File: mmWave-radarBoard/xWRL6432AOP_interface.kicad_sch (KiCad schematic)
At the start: 27 parts, among them U101 MX25R3235FZNxx0, U206 XI6432BRQAAMY, Y101 40MHz

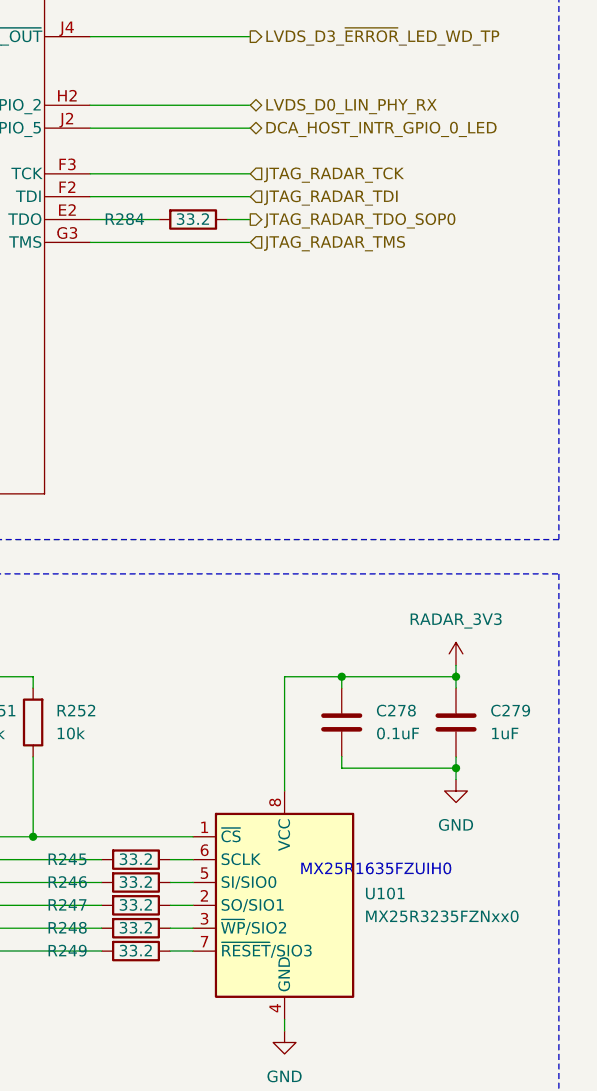
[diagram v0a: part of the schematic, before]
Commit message: Updated schematic of the radar module
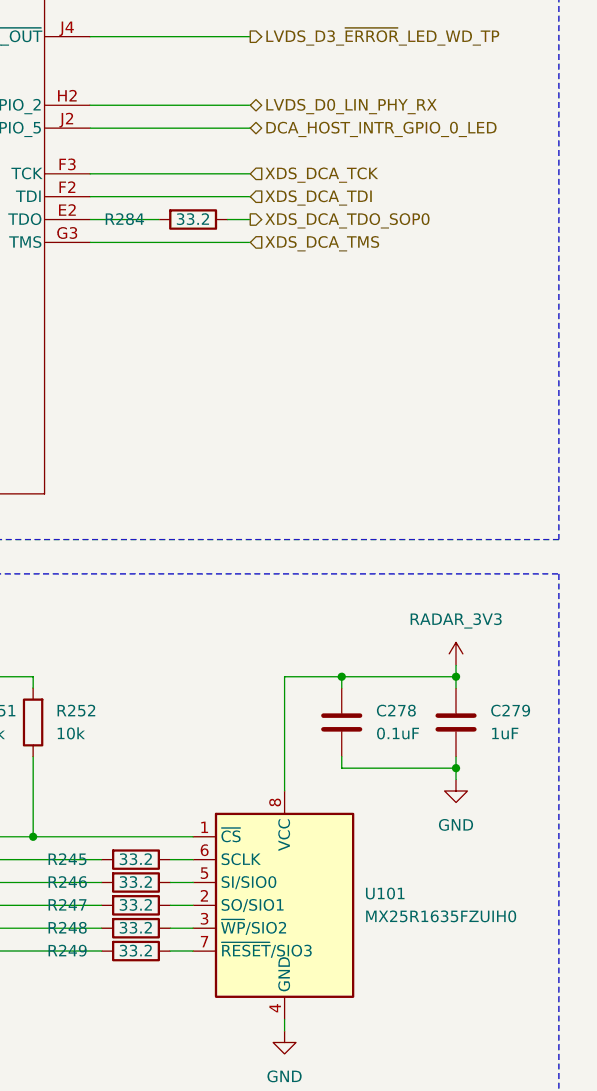
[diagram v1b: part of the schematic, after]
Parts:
- U101: value MX25R3235FZNxx0 -> MX25R1635FZUIH0
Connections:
- net JTAG_RADAR_TCK renamed XDS_DCA_TCK
- net JTAG_RADAR_TDI renamed XDS_DCA_TDI
- net JTAG_RADAR_TDO_SOP0 renamed XDS_DCA_TDO_SOP0
- net JTAG_RADAR_TMS renamed XDS_DCA_TMS
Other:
- note removed: "MX25R1635FZUIH0"
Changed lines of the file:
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@@
 		(company "Designer: EV")
 	)
-	(text "MX25R1635FZUIH0"
-		(exclude_from_sim no)
-		(at 218.44 138.43 0)
-		(effects
-			(font
-				(size 1.27 1.27)
-			)
-		)
-	)
 	(text_box "xWRL6432AOP QSPI flash"
 		(exclude_from_sim no)
@@
 		)
 	)
-	(hierarchical_label "JTAG_RADAR_TDO_SOP0"
+	(hierarchical_label "XDS_DCA_TDO_SOP0"
 		(shape output)
 		(at 204.47 66.04 0)
@@
 		)
 	)
-	(hierarchical_label "JTAG_RADAR_TDI"
+	(hierarchical_label "XDS_DCA_TDI"
 		(shape input)
 		(at 204.47 63.5 0)
@@
 		)
 	)
-	(hierarchical_label "JTAG_RADAR_TMS"
+	(hierarchical_label "XDS_DCA_TMS"
 		(shape input)
 		(at 204.47 68.58 0)
@@
 		)
 	)
-	(hierarchical_label "JTAG_RADAR_TCK"
+	(hierarchical_label "XDS_DCA_TCK"
 		(shape input)
 		(at 204.47 60.96 0)
@@
 			)
 		)
-		(property "Value" "MX25R3235FZNxx0"
+		(property "Value" "MX25R1635FZUIH0"
 			(at 217.17 143.5099 0)
 			(effects

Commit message: Removed unnecessary bits
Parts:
- added D501: LED RED, symbol Device:LED
- added R278: 2.2k, symbol Device:R
- added R279: 0, symbol Device:R
- added TP213, TP214, TP216: TestPoint, symbol Connector:TestPoint
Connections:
- net DCA_FTDI_MOSI renamed FTDI_MOSI
- net DCA_HOST_INTR_GPIO_0_LED renamed HOST_INTR_GPIO_0_LED
- net DCA_SPI_CLK_I2C_SCL renamed SPI_CLK_I2C_SCL
- net DCA_SPI_CLK_I2C_SDA renamed SPI_CLK_I2C_SDA
- net DCA_SPI_MISO_REG_MODE renamed SPI_MISO_REG_MODE
- net LVDS_CLK_RTC_CLKIN_TP renamed RTC_CLK
- net RTC_CLK: now also TP214.1
- net LVDS_D0_LIN_PHY_RX renamed LIN_PHY_RX
- net LVDS_D1_XDS_UARTA_RX_CAN_RX renamed CAN_RX
- net LVDS_D2_XDS_UARTA_TX_CAN_TX renamed CAN_TX
- net LVDS_D3_~{ERROR}_LED_WD_TP renamed ~{ERROR}_LED_WD_TP
- net ~{ERROR}_LED_WD_TP: now also D501.1 (K), R279.1, TP216.1
- net LVDS_FRCLK_HOST_CLK_TP renamed HOST_CLK
- net HOST_CLK: now also TP213.1
- net XDS_DCA_RS232_RX renamed RS232_RX
- net XDS_DCA_RS232_TX renamed RS232_TX
- net XDS_DCA_TCK renamed TCK
- net XDS_DCA_TDI renamed TDI
- net XDS_DCA_TDO_SOP0 renamed TDO_SOP0
- net XDS_DCA_TMS renamed TMS
- new net: D501.2 (A), R278.1
- new net VCC_3V3: R278.2, R279.2

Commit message: Finished schematic
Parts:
- added C502: 10uF, Capacitor_SMD:C_0603_1608Metric, symbol Device:C
- added J501: Conn_02x06_Odd_Even, Connector_JST:JST_PUD_B12B-PUDSS_2x06_P2.00mm_Vertical, symbol Connector_Generic:Conn_02x06_Odd_Even
- C501: renamed from C280; footprint (none) -> Capacitor_SMD:C_0603_1608Metric
- C503: renamed from C278; footprint (none) -> Capacitor_SMD:C_0603_1608Metric
- C504: renamed from C279; footprint (none) -> Capacitor_SMD:C_0603_1608Metric
- C505: renamed from C283; footprint (none) -> Capacitor_SMD:C_0402_1005Metric
- C506: renamed from C281; footprint (none) -> Capacitor_SMD:C_0402_1005Metric
- C507: renamed from C282; footprint (none) -> Capacitor_SMD:C_0402_1005Metric
- D501: footprint (none) -> LED_SMD:LED_0603_1608Metric
- R501: renamed from R253; footprint (none) -> Resistor_SMD:R_0603_1608Metric
- R502: renamed from R278; footprint (none) -> Resistor_SMD:R_0603_1608Metric
- R503: renamed from R279; footprint (none) -> Resistor_SMD:R_0603_1608Metric
- R504: renamed from R284; footprint (none) -> Resistor_SMD:R_0402_1005Metric
- R505: renamed from R254; footprint (none) -> Resistor_SMD:R_0603_1608Metric
- R506: renamed from R255; footprint (none) -> Resistor_SMD:R_0603_1608Metric
- R507: renamed from R250; footprint (none) -> Resistor_SMD:R_0603_1608Metric
- R508: renamed from R251; footprint (none) -> Resistor_SMD:R_0603_1608Metric
- R509: renamed from R252; footprint (none) -> Resistor_SMD:R_0603_1608Metric
- R510: renamed from R256; footprint (none) -> Resistor_SMD:R_0603_1608Metric
- R511: renamed from R257; footprint (none) -> Resistor_SMD:R_0603_1608Metric
- R512: renamed from R258; footprint (none) -> Resistor_SMD:R_0603_1608Metric
- R513: renamed from R245; footprint (none) -> Resistor_SMD:R_0603_1608Metric
- R514: renamed from R246; footprint (none) -> Resistor_SMD:R_0603_1608Metric
- R515: renamed from R247; footprint (none) -> Resistor_SMD:R_0603_1608Metric
- R516: renamed from R248; footprint (none) -> Resistor_SMD:R_0603_1608Metric
- R517: renamed from R249; footprint (none) -> Resistor_SMD:R_0603_1608Metric
- TP501: renamed from TP211; footprint (none) -> TestPoint:TestPoint_Pad_D1.0mm
- TP502: renamed from TP206; footprint (none) -> TestPoint:TestPoint_Pad_D1.0mm
- TP503: renamed from TP213; footprint (none) -> TestPoint:TestPoint_Pad_D1.0mm
- TP504: renamed from TP210; footprint (none) -> TestPoint:TestPoint_Pad_D1.0mm
- TP505: renamed from TP216; footprint (none) -> TestPoint:TestPoint_Pad_D1.0mm
- TP506: renamed from TP214; footprint (none) -> TestPoint:TestPoint_Pad_D1.0mm
- renumbered U101 to U501, Y101 to Y501
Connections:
- net GND: now also C502.1, J501.11 (Pin_11)
- net HOST_INTR_GPIO_0_LED: now also J501.12 (Pin_12)
- net PMIC_CLKOUT_LIN_PHY_TX_SOP1: now also J501.4 (Pin_4)
- net RADAR_3V3: now also C502.2, J501.1 (Pin_1)
- net RADAR_~{RST}: now also J501.10 (Pin_10)
- net RS232_RX: now also J501.9 (Pin_9)
- net RS232_TX: now also J501.3 (Pin_3)
- net SPI_CLK_I2C_SCL: now also J501.7 (Pin_7)
- net SPI_MISO_REG_MODE: now also J501.2 (Pin_2)
- net TDO_SOP0: now also J501.6 (Pin_6)
- net FTDI_MOSI renamed FTDI_SPI_MOSI
- net FTDI_SPI_MOSI: now also J501.8 (Pin_8)
- net SPI_CLK_I2C_SDA renamed SPI_CS_I2C_SDA
- net SPI_CS_I2C_SDA: now also J501.5 (Pin_5)
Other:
- moved on the sheet: C501, C503, C504, C505, C506, C507, R501, R504, R505, R506, R507, R508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

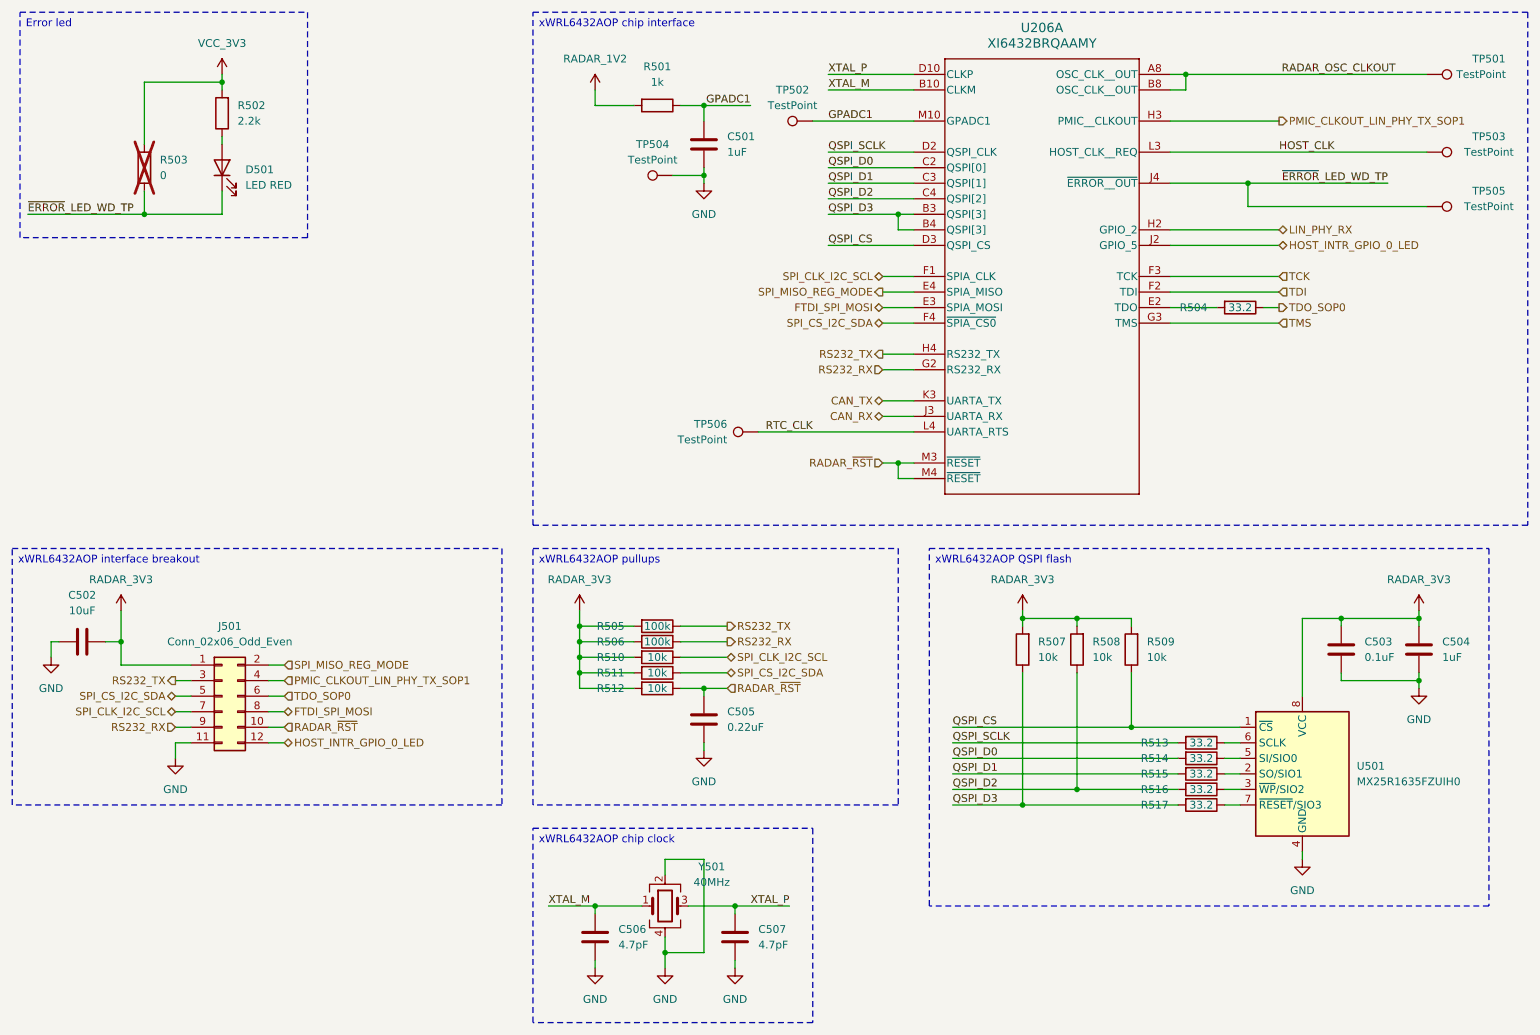
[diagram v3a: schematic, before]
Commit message: Updated schematic and PCB
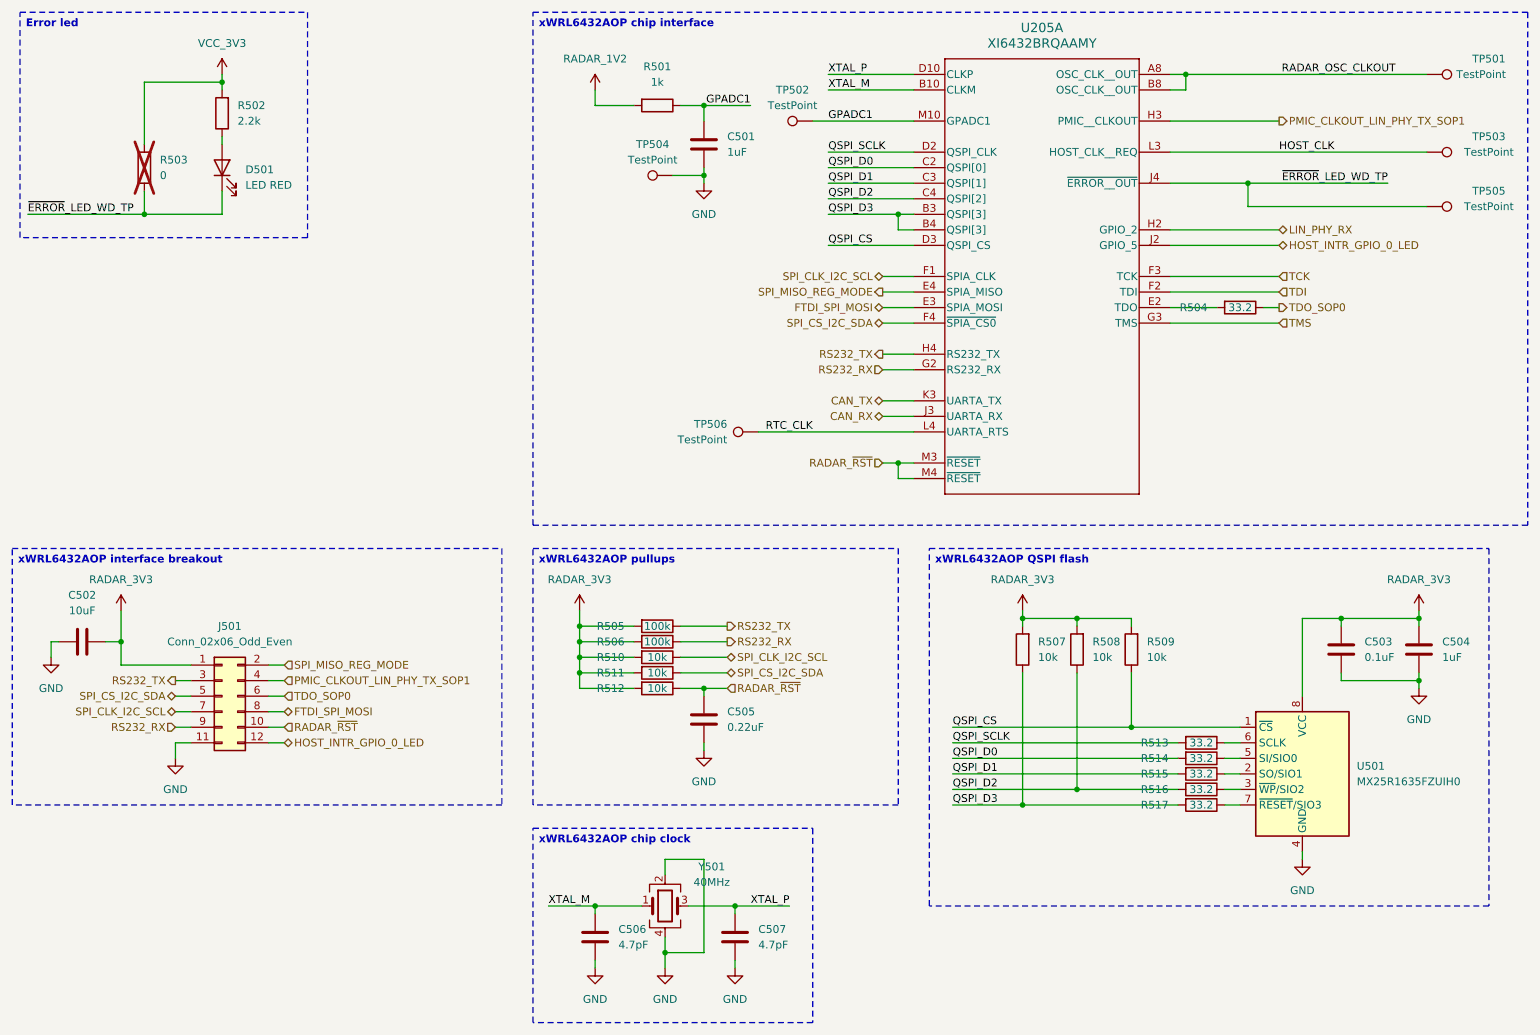
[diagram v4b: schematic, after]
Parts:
- R513, R514, R515, R516, R517: footprint Resistor_SMD:R_0603_1608Metric -> Resistor_SMD:R_0201_0603Metric
- U205: renamed from U206; footprint FCCSP101_AMY_TEX -> XI6432B:FCCSP101_AMY_TEX
- U501: footprint Package_SON:WSON-8-1EP_6x5mm_P1.27mm_EP3.4x4mm -> MX25R1635FZUIH0:PSON50P200X300X60-9N
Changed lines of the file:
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@@
 	(title_block
 		(title "xWRL6432AOP interface")
-		(date "2025-04-14")
+		(date "2025-04-20")
 		(rev "V1.0")
 		(company "Designer: EV")
@@
 			(font
 				(size 1.27 1.27)
+				(thickness 0.254)
+				(bold yes)
 			)
 			(justify left top)
@@
 			(font
 				(size 1.27 1.27)
+				(thickness 0.254)
+				(bold yes)
 			)
 			(justify left top)
@@
 			(font
 				(size 1.27 1.27)
+				(thickness 0.254)
+				(bold yes)
 			)
 			(justify left top)
@@
 			(font
 				(size 1.27 1.27)
+				(thickness 0.254)
+				(bold yes)
 			)
 			(justify left top)
@@
 			(font
 				(size 1.27 1.27)
+				(thickness 0.254)
+				(bold yes)
 			)
 			(justify left top)
@@
 			(font
 				(size 1.27 1.27)
+				(thickness 0.254)
+				(bold yes)
 			)
 			(justify left top)
@@
 			)
 		)
-		(property "Footprint" "Resistor_SMD:R_0603_1608Metric"
+		(property "Footprint" "Resistor_SMD:R_0201_0603Metric"
 			(at 222.25 145.542 90)
 			(effects
@@
 			)
 		)
-		(property "Footprint" "Resistor_SMD:R_0603_1608Metric"
+		(property "Footprint" "Resistor_SMD:R_0201_0603Metric"
 			(at 222.25 135.382 90)
 			(effects
@@
 			)
 		)
-		(property "Footprint" "Resistor_SMD:R_0603_1608Metric"
+		(property "Footprint" "Resistor_SMD:R_0201_0603Metric"
 			(at 222.25 143.002 90)
 			(effects
@@
 		(dnp no)
 		(fields_autoplaced yes)
-		(property "Reference" "U206"
+		(property "Reference" "U205"
 			(at 196.215 20.32 0)
 			(effects
@@
 			)
 		)
-		(property "Footprint" "FCCSP101_AMY_TEX"
+		(property "Footprint" "XI6432B:FCCSP101_AMY_TEX"
 			(at 195.58 148.59 0)
 			(effects
@@
 			(project "mmWave-radarBoard"
 				(path "/65d1bf45-0c7d-403c-8da5-e1777d98e937/67383843-b151-490b-b925-303d04bb18ba"
-					(reference "U206")
+					(reference "U205")
 					(unit 1)
 				)
@@
 			)
 		)
-		(property "Footprint" "Resistor_SMD:R_0603_1608Metric"
+		(property "Footprint" "Resistor_SMD:R_0201_0603Metric"
 			(at 222.25 140.462 90)
 			(effects
@@
 			)
 		)
-		(property "Footprint" "Package_SON:WSON-8-1EP_6x5mm_P1.27mm_EP3.4x4mm"
+		(property "Footprint" "MX25R1635FZUIH0:PSON50P200X300X60-9N"
 			(at 238.76 157.48 0)
 			(effects
@@
 			)
 		)
-		(property "Footprint" "Resistor_SMD:R_0603_1608Metric"
+		(property "Footprint" "Resistor_SMD:R_0201_0603Metric"
 			(at 222.25 137.922 90)
 			(effects

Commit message: Updated schematic and PCB
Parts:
- C501: footprint Capacitor_SMD:C_0603_1608Metric -> Capacitor_SMD:C_0402_1005Metric
- R501: footprint Resistor_SMD:R_0603_1608Metric -> Resistor_SMD:R_0402_1005Metric
- R505, R506, R510, R511, R512: footprint Resistor_SMD:R_0603_1608Metric -> Resistor_SMD:R_0201_0603Metric
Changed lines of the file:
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@@
 			)
 		)
-		(property "Footprint" "Resistor_SMD:R_0603_1608Metric"
+		(property "Footprint" "Resistor_SMD:R_0201_0603Metric"
 			(at 133.35 126.492 90)
 			(effects
@@
 			)
 		)
-		(property "Footprint" "Resistor_SMD:R_0603_1608Metric"
+		(property "Footprint" "Resistor_SMD:R_0201_0603Metric"
 			(at 133.35 118.872 90)
 			(effects
@@
 			)
 		)
-		(property "Footprint" "Resistor_SMD:R_0603_1608Metric"
+		(property "Footprint" "Resistor_SMD:R_0201_0603Metric"
 			(at 133.35 116.332 90)
 			(effects
@@
 			)
 		)
-		(property "Footprint" "Resistor_SMD:R_0603_1608Metric"
+		(property "Footprint" "Resistor_SMD:R_0201_0603Metric"
 			(at 133.35 123.952 90)
 			(effects
@@
 			)
 		)
-		(property "Footprint" "Resistor_SMD:R_0603_1608Metric"
+		(property "Footprint" "Resistor_SMD:R_0402_1005Metric"
 			(at 133.35 31.242 90)
 			(effects
@@
 			)
 		)
-		(property "Footprint" "Capacitor_SMD:C_0603_1608Metric"
+		(property "Footprint" "Capacitor_SMD:C_0402_1005Metric"
 			(at 141.9352 43.18 0)
 			(effects
@@
 			)
 		)
-		(property "Footprint" "Resistor_SMD:R_0603_1608Metric"
+		(property "Footprint" "Resistor_SMD:R_0201_0603Metric"
 			(at 133.35 121.412 90)
 			(effects

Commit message: Updated PCB
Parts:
- C503: footprint Capacitor_SMD:C_0603_1608Metric -> Capacitor_SMD:C_0402_1005Metric
- R505, R506, R510, R511, R512, R513, R514, R515, R516, R517: footprint Resistor_SMD:R_0201_0603Metric -> Resistor_SMD:R_0402_1005Metric
- R507, R508, R509: footprint Resistor_SMD:R_0603_1608Metric -> Resistor_SMD:R_0402_1005Metric
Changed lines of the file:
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@@
 			)
 		)
-		(property "Footprint" "Resistor_SMD:R_0201_0603Metric"
+		(property "Footprint" "Resistor_SMD:R_0402_1005Metric"
 			(at 133.35 126.492 90)
 			(effects
@@
 			)
 		)
-		(property "Footprint" "Resistor_SMD:R_0603_1608Metric"
+		(property "Footprint" "Resistor_SMD:R_0402_1005Metric"
 			(at 194.818 121.92 90)
 			(effects
@@
 			)
 		)
-		(property "Footprint" "Resistor_SMD:R_0201_0603Metric"
+		(property "Footprint" "Resistor_SMD:R_0402_1005Metric"
 			(at 222.25 145.542 90)
 			(effects
@@
 			)
 		)
-		(property "Footprint" "Resistor_SMD:R_0201_0603Metric"
+		(property "Footprint" "Resistor_SMD:R_0402_1005Metric"
 			(at 222.25 135.382 90)
 			(effects
@@
 			)
 		)
-		(property "Footprint" "Resistor_SMD:R_0201_0603Metric"
+		(property "Footprint" "Resistor_SMD:R_0402_1005Metric"
 			(at 133.35 118.872 90)
 			(effects
@@
 			)
 		)
-		(property "Footprint" "Resistor_SMD:R_0201_0603Metric"
+		(property "Footprint" "Resistor_SMD:R_0402_1005Metric"
 			(at 222.25 143.002 90)
 			(effects
@@
 			)
 		)
-		(property "Footprint" "Resistor_SMD:R_0201_0603Metric"
+		(property "Footprint" "Resistor_SMD:R_0402_1005Metric"
 			(at 133.35 116.332 90)
 			(effects
@@
 			)
 		)
-		(property "Footprint" "Resistor_SMD:R_0201_0603Metric"
+		(property "Footprint" "Resistor_SMD:R_0402_1005Metric"
 			(at 222.25 140.462 90)
 			(effects
@@
 			)
 		)
-		(property "Footprint" "Resistor_SMD:R_0201_0603Metric"
+		(property "Footprint" "Resistor_SMD:R_0402_1005Metric"
 			(at 133.35 123.952 90)
 			(effects
@@
 			)
 		)
-		(property "Footprint" "Resistor_SMD:R_0603_1608Metric"
+		(property "Footprint" "Resistor_SMD:R_0402_1005Metric"
 			(at 212.598 121.92 90)
 			(effects
@@
 			)
 		)
-		(property "Footprint" "Capacitor_SMD:C_0603_1608Metric"
+		(property "Footprint" "Capacitor_SMD:C_0402_1005Metric"
 			(at 246.0752 125.73 0)
 			(effects
@@
 			)
 		)
-		(property "Footprint" "Resistor_SMD:R_0201_0603Metric"
+		(property "Footprint" "Resistor_SMD:R_0402_1005Metric"
 			(at 133.35 121.412 90)
 			(effects
@@
 			)
 		)
-		(property "Footprint" "Resistor_SMD:R_0201_0603Metric"
+		(property "Footprint" "Resistor_SMD:R_0402_1005Metric"
 			(at 222.25 137.922 90)
 			(effects
@@
 			)
 		)
-		(property "Footprint" "Resistor_SMD:R_0603_1608Metric"
+		(property "Footprint" "Resistor_SMD:R_0402_1005Metric"
 			(at 203.708 121.92 90)
 			(effects

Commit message: Updated schematic and layout PCB
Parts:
- renumbered C501 to C90, C502 to C91, C503 to C92, C504 to C93, C505 to C94, C506 to C95, C507 to C96, D501 to D10, J501 to J9, R501 to R60, R502 to R61, R503 to R62, R504 to R63, R505 to R64, R506 to R65, R507 to R66, R508 to R67, R509 to R68, R510 to R69, R511 to R70, R512 to R71, R513 to R72, R514 to R73, R515 to R74, R516 to R75, R517 to R76, TP502 to TP10, TP503 to TP11, TP504 to TP12, TP505 to TP13, TP506 to TP14, TP501 to TP9, U501 to U12, U205 to U5, Y501 to Y2
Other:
- title: xWRL6432AOP interface -> Power
